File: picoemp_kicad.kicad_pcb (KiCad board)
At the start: 2 copper layers, 40 x 116 mm, 98 parts, among them J1 EDGE-SMA, J2 USB_C_Receptacle_USB2.0, J3 BG306-02-A-2-0400-L-G, J4 Conn_01x02_Pin, P2 Header 2, P3 Header 4, Q1 LDA111STR, Q2 RGT16BM65DTL, Q3 AO3422, Q4 AO3422, Q5 FSS2301S, Q6 FSS2302S, SW1 ARM, SW2 PULSE, SW3 TL3301AF160QJ, SW4 SW_SPST, T1 ATB322524, T2 ATB322524, U1 RP2040, U2 W25Q128JVSIQ, U3 TP4056, U4 DW01A, U5 FS8205A, U6 LP2985-3.3, Y1 X322512MSB4SI

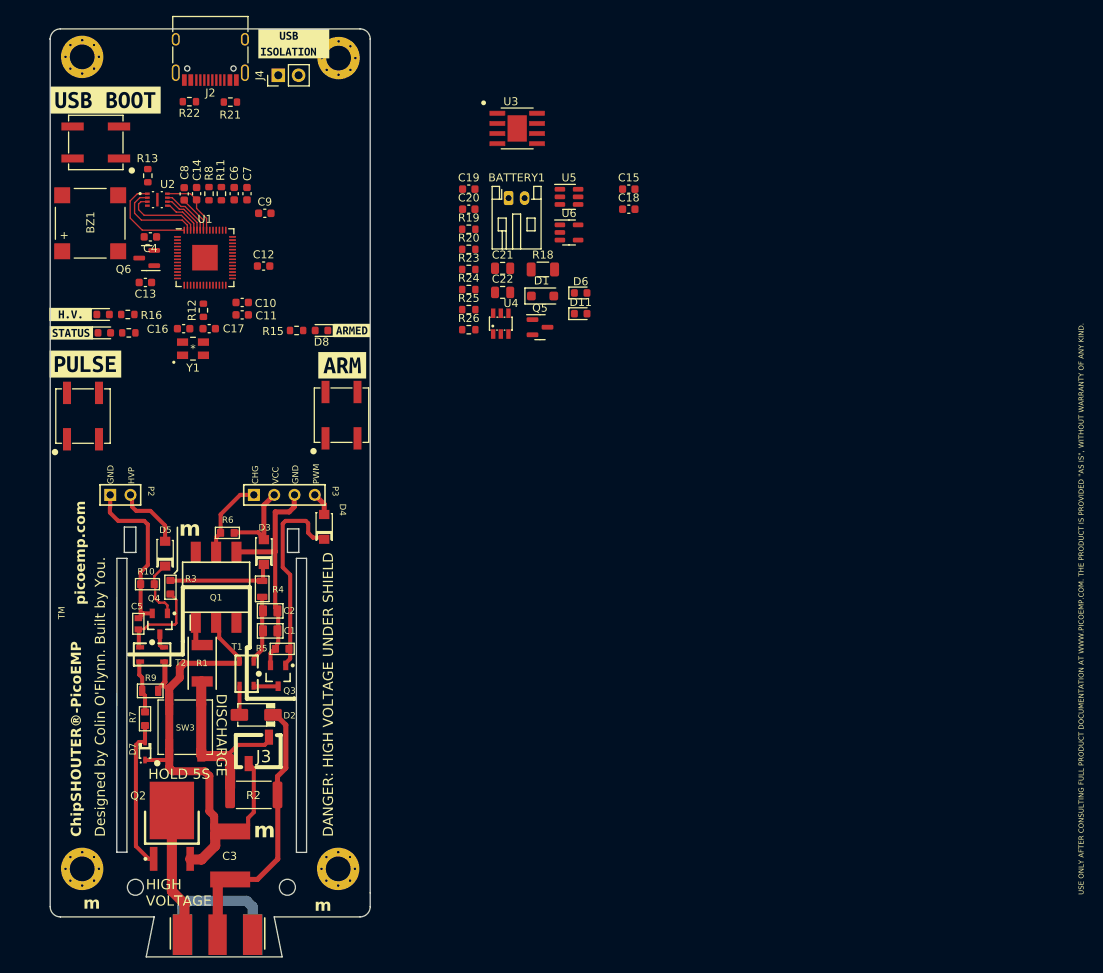
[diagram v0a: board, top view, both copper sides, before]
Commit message: Swapped charging IC for reduced footprint
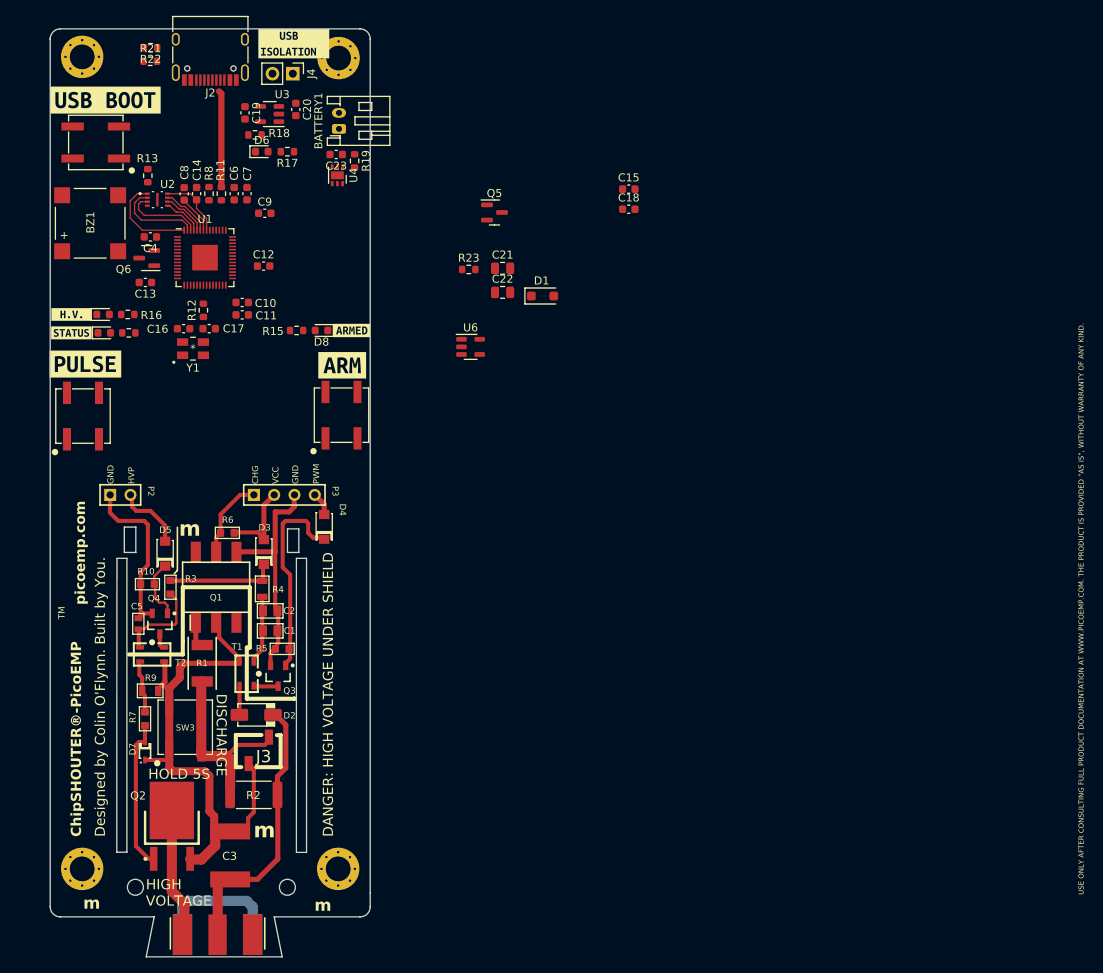
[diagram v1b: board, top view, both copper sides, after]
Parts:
- removed D11: CHARGING, LED_SMD:LED_0603_1608Metric
- removed R20, R24, R26: 1k, Resistor_SMD:R_0603_1608Metric
- removed R25: 100, Resistor_SMD:R_0603_1608Metric
- removed U5: FS8205A, Package_TO_SOT_SMD:SOT-23-6
- removed kibuzzard-63F26E94: G***, kibuzzard-63F26E94
- removed kibuzzard-63F26F80: G***, kibuzzard-63F26F80
- added C23: 100n, Capacitor_SMD:C_0603_1608Metric, F.Cu at (164.3, 62.7)
- added R17: 2k, Resistor_SMD:R_0603_1608Metric, F.Cu at (158.2, 62.4)
- added kibuzzard-63F48B50: G***, kibuzzard-63F48B50, F.Cu at (131.2, 82.7)
- added kibuzzard-63F48B5A: G***, kibuzzard-63F48B5A, F.Cu at (131.2, 85.0)
- C20: value 0.1u -> 10u
- D6: value CHARGING_COMPLETE -> CHARGING
- R18: value 0.4 -> 2k; footprint Resistor_SMD:R_1206_3216Metric -> Resistor_SMD:R_0603_1608Metric
- R19: value 2.2k -> 100
- U3: value TP4056 -> LP4054H; footprint LCSC:SOP127P600X175-9N -> Package_TO_SOT_SMD:SOT-23-5
- U4: value DW01A -> XB6536A; footprint LCSC:SOT23-6 -> Package_DFN_QFN:DFN-6-1EP_2x2mm_P0.65mm_EP1x1.6mm
- moved D6 43.6 mm to (155.0, 62.4)
- moved R18 39.7 mm to (154.1, 60.3), turned to 180 degrees
- moved U3 31.0 mm to (156.0, 57.7), turned to 180 degrees
- moved C19 29.6 mm to (152.9, 57.5), turned to -90 degrees
- moved U4 27.6 mm to (164.4, 65.3), turned to -90 degrees
- moved C20 25.0 mm to (159.2, 57.1), turned to -90 degrees
- moved BATTERY1 22.9 mm to (164.6, 59.5), turned to 90 degrees
- moved U6 18.9 mm to (181.1, 86.8)
- moved R19 16.6 mm to (166.6, 63.5), turned to -90 degrees
- moved Q5 15.4 mm to (184.0, 70.0)
- moved R21 11.2 mm to (141.0, 51.1), turned to 180 degrees
- moved R22 8.31 mm to (141.1, 49.4)
- moved J4 1.83 mm to (158.8, 52.6), turned to -90 degrees
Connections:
- C19 pad 1: /Power/BAT+ -> +5V
- C20 pad 1: Net-(U4-VCC) -> Net-(U3-BAT)
- C20 pad 2: /Power/BAT- -> GND
- D6 pad 2: +5V -> Net-(D6-A)
- R18 pad 1: Net-(U3-VCC) -> Net-(U3-ISET)
- R18 pad 2: +5V -> GND
- R19 pad 1: Net-(U3-PROG) -> /Power/BAT+
- R19 pad 2: GND -> Net-(U4-VDD)
- U3 pad 1: GND -> Net-(D6-K)
- U3 pad 2: Net-(U3-PROG) -> GND
- U3 pad 3: GND -> Net-(U3-BAT)
- U3 pad 4: Net-(U3-VCC) -> +5V
- U3 pad 5: /Power/BAT+ -> Net-(U3-ISET)
- U4 pad 1: Net-(U4-OD) -> Net-(U4-VDD)
- U4 pad 2: Net-(U4-CS) -> /Power/BAT-
- U4 pad 3: Net-(U4-OC) -> /Power/BAT-
- U4 pad 4: unconnected-(U4-TD-Pad4) -> GND
- U4 pad 5: Net-(U4-VCC) -> GND
- U4 pad 6: /Power/BAT- -> GND
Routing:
- net USB_D-: track 0.00 -> 12.1 mm

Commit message: finalized schematic + layout
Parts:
- removed MH2, MH3 (x2): M3, Tight Fit, C:_Users_colin_Dropbox (NewAE Technology Inc)_engineering_altium_Libraries_footprints_MOUNT_M3_TIGHT.PcbLib_MOUNT_M3_TI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
- removed kibuzzard-63F119CF: G***, kibuzzard-63F119CF
- removed kibuzzard-63F26FC0: G***, kibuzzard-63F26FC0
- removed kibuzzard-63F48B50: G***, kibuzzard-63F48B50
- removed kibuzzard-63F48B5A: G***, kibuzzard-63F48B5A
- added C24: 10u, Capacitor_SMD:C_0603_1608Metric, F.Cu at (158.2, 53.1)
- added D10: PICO_LED1, LED_SMD:LED_0603_1608Metric, F.Cu at (156.1, 82.0)
- added D11: LESD9L5.0T5G, Diode_SMD:D_SOD-923, F.Cu at (150.2, 55.2)
- added D13: LESD9L5.0T5G, Diode_SMD:D_SOD-923, F.Cu at (148.1, 55.2)
- added D14: PESDNC5D7VU, Diode_SMD:D_SOD-523, F.Cu at (141.1, 51.2)
- added G***: LOGO, LOGO, F.Cu at (136.3, 155.2)
- added G***: LOGO, LOGO, F.Cu at (160.8, 155.2)
- added G***: LOGO, LOGO, F.Cu at (156.3, 149.1)
- added G***: LOGO, LOGO, F.Cu at (146.8, 108.5)
- added G***: LOGO, LOGO, B.Cu at (149.5, 160.0)
- added J5: Conn_01x03_Socket, Connector_PinHeader_2.54mm:PinHeader_1x03_P2.54mm_Vertical, F.Cu at (154.0, 94.5)
- added J6: Conn_01x08_Socket, Connector_PinSocket_2.54mm:PinSocket_1x08_P2.54mm_Vertical, F.Cu at (130.4, 59.5)
- added MH1: M3, Tight Fit, C:_Users_colin_Dropbox (NewAE Technology Inc)_engineering_altium_Libraries_footprints_MOUNT_M3_TIGHT.PcbLib_MOUNT_M3_TI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, F.Cu at (164.5, 114.7)
- added MH1: M3, Tight Fit, C:_Users_colin_Dropbox (NewAE Technology Inc)_engineering_altium_Libraries_footprints_MOUNT_M3_TIGHT.PcbLib_MOUNT_M3_TI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, F.Cu at (132.5, 114.7)
- added MH1: M3, Tight Fit, C:_Users_colin_Dropbox (NewAE Technology Inc)_engineering_altium_Libraries_footprints_MOUNT_M3_TIGHT.PcbLib_MOUNT_M3_TI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, F.Cu at (164.5, 152.0)
- added MH1: M3, Tight Fit, C:_Users_colin_Dropbox (NewAE Technology Inc)_engineering_altium_Libraries_footprints_MOUNT_M3_TIGHT.PcbLib_MOUNT_M3_TI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, F.Cu at (164.5, 50.5)
- added MH1: M3, Tight Fit, C:_Users_colin_Dropbox (NewAE Technology Inc)_engineering_altium_Libraries_footprints_MOUNT_M3_TIGHT.PcbLib_MOUNT_M3_TI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, F.Cu at (132.5, 50.5)
- added R20: 1k, Resistor_SMD:R_0603_1608Metric, F.Cu at (156.1, 79.0)
- added SW5: SSSS811101, Button_Switch_SMD:SW_SPDT_PCM12, F.Cu at (166.5, 77.7)
- added U5: ME2807, Package_TO_SOT_SMD:SOT-23-3, F.Cu at (166.6, 68.9)
- added U7: LPW5206, Package_TO_SOT_SMD:SOT-23-5, F.Cu at (155.8, 53.7)
- added kibuzzard-63F6135F: G***, kibuzzard-63F6135F, F.Cu at (161.7, 54.6)
- added kibuzzard-63F6135F: G***, kibuzzard-63F6135F, B.Cu at (163.2, 55.8)
- added kibuzzard-63F61A8A: G***, kibuzzard-63F61A8A, F.Cu at (144.5, 92.2)
- added kibuzzard-63F629BA: G***, kibuzzard-63F629BA, F.Cu at (166.0, 72.2)
- added kibuzzard-63F65118: G***, kibuzzard-63F65118, F.Cu at (166.4, 64.7)
- added kibuzzard-63F66756: G***, kibuzzard-63F66756, F.Cu at (140.9, 55.3)
- added kibuzzard-63F66885: G***, kibuzzard-63F66885, F.Cu at (133.8, 59.5)
- added kibuzzard-63F6689E: G***, kibuzzard-63F6689E, F.Cu at (133.8, 62.0)
- added kibuzzard-63F668C9: G***, kibuzzard-63F668C9, F.Cu at (133.9, 77.2)
- added kibuzzard-63F668D5: G***, kibuzzard-63F668D5, F.Cu at (133.8, 74.7)
- added kibuzzard-63F668E9: G***, kibuzzard-63F668E9, F.Cu at (133.8, 64.5)
- added kibuzzard-63F668EF: G***, kibuzzard-63F668EF, F.Cu at (133.8, 67.0)
- added kibuzzard-63F668F6: G***, kibuzzard-63F668F6, F.Cu at (133.8, 69.6)
- added kibuzzard-63F668FC: G***, kibuzzard-63F668FC, F.Cu at (133.8, 72.2)
- added kibuzzard-63F78DFD: G***, kibuzzard-63F78DFD, F.Cu at (167.5, 62.4)
- added kibuzzard-63F78E1E: G***, kibuzzard-63F78E1E, F.Cu at (167.7, 54.6)
- added kibuzzard-63F78E1E: G***, kibuzzard-63F78E1E, B.Cu at (163.8, 57.5)
- added kibuzzard-63FA0F3A: G***, kibuzzard-63FA0F3A, F.Cu at (131.0, 82.7)
- added kibuzzard-63FA1685: G***, kibuzzard-63FA1685, F.Cu at (158.2, 82.7)
- added kibuzzard-63FA16E2: G***, kibuzzard-63FA16E2, F.Cu at (154.7, 87.3)
- added kibuzzard-63FA16E2: G***, kibuzzard-63FA16E2, B.Cu at (154.7, 87.3)
- added kibuzzard-63FA1A3D: G***, kibuzzard-63FA1A3D, F.Cu at (131.0, 85.0)
- added kibuzzard-63FB2541: G***, kibuzzard-63FB2541, B.Cu at (133.9, 59.5)
- added kibuzzard-63FB254D: G***, kibuzzard-63FB254D, B.Cu at (133.9, 62.0)
- added kibuzzard-63FB2554: G***, kibuzzard-63FB2554, B.Cu at (133.9, 64.5)
- added kibuzzard-63FB255A: G***, kibuzzard-63FB255A, B.Cu at (133.9, 67.0)
- added kibuzzard-63FB2562: G***, kibuzzard-63FB2562, B.Cu at (133.9, 69.6)
- added kibuzzard-63FB2568: G***, kibuzzard-63FB2568, B.Cu at (133.9, 72.2)
- added kibuzzard-63FB256F: G***, kibuzzard-63FB256F, B.Cu at (133.9, 74.7)
- added kibuzzard-63FB2575: G***, kibuzzard-63FB2575, B.Cu at (133.8, 77.2)
- added kibuzzard-63FB2610: G***, kibuzzard-63FB2610, F.Cu at (161.6, 101.8)
- added kibuzzard-63FB2610: G***, kibuzzard-63FB2610, B.Cu at (161.6, 101.8)
- added kibuzzard-63FB2711: G***, kibuzzard-63FB2711, F.Cu at (136.0, 101.8)
- added kibuzzard-63FB2711: G***, kibuzzard-63FB2711, F.Cu at (159.1, 101.8)
- added kibuzzard-63FB2711: G***, kibuzzard-63FB2711, B.Cu at (136.0, 101.8)
- added kibuzzard-63FB2711: G***, kibuzzard-63FB2711, B.Cu at (159.1, 101.8)
- added kibuzzard-63FB271A: G***, kibuzzard-63FB271A, F.Cu at (156.5, 101.8)
- added kibuzzard-63FB271A: G***, kibuzzard-63FB271A, B.Cu at (156.5, 101.8)
- added kibuzzard-63FB2724: G***, kibuzzard-63FB2724, F.Cu at (153.9, 101.8)
- added kibuzzard-63FB2724: G***, kibuzzard-63FB2724, B.Cu at (153.9, 101.8)
- added kibuzzard-63FB2766: G***, kibuzzard-63FB2766, F.Cu at (138.6, 101.8)
- added kibuzzard-63FB2766: G***, kibuzzard-63FB2766, B.Cu at (138.5, 101.8)
- added kibuzzard-63FB287B: G***, kibuzzard-63FB287B, F.Cu at (158.2, 89.4)
- added kibuzzard-63FB2882: G***, kibuzzard-63FB2882, F.Cu at (157.4, 92.0)
- added kibuzzard-63FB2887: G***, kibuzzard-63FB2887, F.Cu at (158.2, 94.6)
- added kibuzzard-63FB2899: G***, kibuzzard-63FB2899, B.Cu at (158.2, 89.4)
- added kibuzzard-63FB28A8: G***, kibuzzard-63FB28A8, B.Cu at (157.4, 92.0)
- added kibuzzard-63FB28B5: G***, kibuzzard-63FB28B5, B.Cu at (158.2, 94.6)
- added kibuzzard-63FB3D52: G***, kibuzzard-63FB3D52, B.Cu at (163.8, 59.3)
- added kibuzzard-63FB718C: G***, kibuzzard-63FB718C, F.Cu at (157.7, 47.8)
- BZ1: value Buzzer -> MLT-7525
- C4: value 100m -> 100n
- D1: value RB161MM-20TR -> DS14W
- D3, D4, D5: value SM4005PL-TP -> GOODWORK A7
- R2: value 300K -> 360k
- U6: value LP2985-3.3 -> LP3992-3.3
- moved C18 58.0 mm to (143.0, 66.1), turned to 180 degrees
- moved C15 46.3 mm to (154.8, 72.0)
- moved D1 32.7 mm to (159.4, 69.3), turned to 90 degrees
- moved BZ1 29.5 mm to (146.2, 97.9), turned to 180 degrees
- moved R23 24.8 mm to (157.3, 69.3), turned to -90 degrees
- moved C22 24.7 mm to (161.2, 73.9)
- moved C21 24.1 mm to (161.2, 80.3)
- moved U6 22.1 mm to (161.2, 77.1), turned to 90 degrees
- moved Q5 21.4 mm to (162.6, 69.3)
- moved Q6 17.9 mm to (149.7, 91.1), turned to 0 degrees
- moved D6 8.21 mm to (162.8, 64.7), turned to 180 degrees
- moved U4 7.93 mm to (157.9, 60.8), turned to 180 degrees
- moved SW4 6.86 mm to (140.9, 59.5), turned to 0 degrees
- moved C23 5.58 mm to (158.7, 62.8)
- moved R27 5.05 mm to (137.7, 80.0), turned to -90 degrees
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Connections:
- net Net-(J4-Pin_2) renamed /Power/VBUS
- C20 pad 1: Net-(U3-BAT) -> /Power/BAT+
- C21 pad 1: +5V -> /Power/VOUT
- D3 pad A: VCC -> +3V3
- J4 pad 1: +5V -> Net-(J4-Pin_1)
- P3 pad 2: VCC -> +3V3
- R6 pad 1: VCC -> +3V3
- SW2 pad 1: /RP2040/PULSE_BUTTON -> +3V3
- SW2 pad 2: +3V3 -> /RP2040/PULSE_BUTTON
- U1 pad 18: unconnected-(U1-GPIO15-Pad18) -> /RP2040/BUZZER
- U1 pad 2: unconnected-(U1-GPIO0-Pad2) -> /RP2040/GPIO0
- U1 pad 24: unconnected-(U1-SWCLK-Pad24) -> /RP2040/SWCLK
- U1 pad 25: unconnected-(U1-SWDIO-Pad25) -> /RP2040/SWDIO
- U1 pad 3: unconnected-(U1-GPIO1-Pad3) -> /RP2040/GPIO1
- U1 pad 37: unconnected-(U1-GPIO25-Pad37) -> /RP2040/PICO_LED
- U1 pad 39: unconnected-(U1-GPIO27/ADC1-Pad39) -> /RP2040/ARMED_LED
- U1 pad 4: unconnected-(U1-GPIO2-Pad4) -> /RP2040/GPIO2
- U1 pad 5: unconnected-(U1-GPIO3-Pad5) -> /RP2040/GPIO3
- U1 pad 6: /RP2040/BUZZER -> /RP2040/GPIO4
- U1 pad 7: unconnected-(U1-GPIO5-Pad7) -> /RP2040/GPIO5
- U3 pad 3: Net-(U3-BAT) -> /Power/BAT+
- U6 pad 1: +5V -> /Power/VOUT
- U6 pad 3: +5V -> /Power/LDO_ENABLE
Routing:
- net +3V3: track 8.28 -> 167.4 mm, vias 0 -> 4
- net GND: track 50.5 -> 95.9 mm, vias 0 -> 66
- net CHARGED: track 9.73 -> 44.8 mm
- net /RP2040/ARM_BUTTON: track 0.00 -> 32.5 mm
- net HVPWM: track 2.93 -> 35.5 mm
- net HVPULSE: track 8.83 -> 38.9 mm
- net +5V: track 0.00 -> 26.6 mm
- net /RP2040/PULSE_BUTTON: track 0.00 -> 26.4 mm
- net +1V1: track 4.76 -> 29.9 mm, vias 0 -> 4
- net /Power/VOUT: track 0.00 -> 24.7 mm
- net /RP2040/GPIO0: track 0.00 -> 24.0 mm
- net /RP2040/GPIO1: track 0.00 -> 22.0 mm
- net /Power/VBUS: track 0.00 -> 21.1 mm
- net /RP2040/GPIO2: track 0.00 -> 20.1 mm
- net /RP2040/SWCLK: track 0.00 -> 18.8 mm
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- added copper zone on F.Cu, net +3V3
- added copper zone on F.Cu, net /Power/BAT+
- added copper zone on F.Cu, net /Power/BAT-
- added copper zone on B.Cu, net GND
- added copper zone on F.Cu, net GND
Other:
- board text added: "USE ONLY AFTER CONSULTING FULL PRODUCT DOCUMENTATION AT WWW.PICOEMP.COM THE PRODUCT IS PROVIDED {dblquote}AS IS{dblquote}, WITHOUT WARRANTY OF ANY KIND."
- board text removed: "CHG"
- board text removed: "Designed by Colin O'Flynn. Built by You."
- board text removed: "GND"
- board text removed: "HVP"
- board text removed: "PWM"
- board text removed: "USE ONLY AFTER CONSULTING FULL PRODUCT DOCUMENTATION AT WWW.PICOEMP.COM. THE PRODUCT IS PROVIDED "AS IS", WITHOUT WARRANTY OF ANY KIND."
- board text removed: "VCC"
- board text removed: "m"
- board text removed: "picoemp.com"

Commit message: Small tweaks
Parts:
- added G***: LOGO, LOGO, F.Cu at (135.3, 145.7)
- added G***: LOGO, LOGO, F.Cu at (130.2, 127.7)

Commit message: finishing touches
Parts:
- removed J4: Conn_01x02_Pin, Connector_PinHeader_2.54mm:PinHeader_1x02_P2.54mm_Vertical
- removed the MH1 at (164.5, 50.5)
- removed kibuzzard-63F2728F: G***, kibuzzard-63F2728F
- removed kibuzzard-63FB718C: G***, kibuzzard-63FB718C
- added D15: 5V_PWR, LED_SMD:LED_0603_1608Metric, F.Cu at (134.2, 55.2)
- added G***: LOGO, LOGO, B.Cu at (162.7, 133.3)
- added G***: LOGO, LOGO, B.Cu at (147.6, 133.3)
- added JP1: ~, Jumper:SolderJumper-2_P1.3mm_Open_Pad1.0x1.5mm, B.Cu at (155.1, 52.3)
- added Q7: FSS2302S, Package_TO_SOT_SMD:SOT-23, F.Cu at (158.1, 49.7)
- added R24: 1k, Resistor_SMD:R_0603_1608Metric, F.Cu at (141.1, 48.2)
- added R25: 100k, Resistor_SMD:R_0603_1608Metric, F.Cu at (154.7, 49.7)
- added R26: 100k, Resistor_SMD:R_0603_1608Metric, F.Cu at (143.5, 90.1)
- added REF**: MountingHole_3.2mm_M3_Pad_TopOnly, MountingHole:MountingHole_3.2mm_M3_Pad_TopOnly, F.Cu at (164.5, 50.5)
- added SW6: SSSS811101, Button_Switch_SMD:SW_SPDT_PCM12, B.Cu at (157.9, 49.1)
- added kibuzzard-63FF3009: G***, kibuzzard-63FF3009, F.Cu at (166.2, 85.0)
- added kibuzzard-640062E5: G***, kibuzzard-640062E5, B.Cu at (154.6, 133.3)
- added kibuzzard-640065CA: G***, kibuzzard-640065CA, F.Cu at (130.6, 55.2)
- added kibuzzard-64031476: G***, kibuzzard-64031476, B.Cu at (165.5, 47.8)
- added kibuzzard-640384C5: G***, kibuzzard-640384C5, F.Cu at (149.7, 134.4)
- added kibuzzard-640385A5: G***, kibuzzard-640385A5, F.Cu at (148.6, 143.1)
- added kibuzzard-6403912E: G***, kibuzzard-6403912E, B.Cu at (154.8, 60.3)
- C3: footprint C:_Users_cofly_Dropbox (NewAE Technology Inc)_engineering_altium_Libraries_footprints_CKG57N_2220.PcbLib_CKG57N_2220 -> Capacitor_SMD:C_2220_5650Metric
- moved G*** 1.39 mm to (135.3, 144.3)
- moved G*** 1.39 mm to (130.3, 126.3)
- moved C3 0.81 mm to (151.4, 151.0), turned to 90 degrees
- moved G*** 0.35 mm to (156.7, 149.0)
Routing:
- net +5V: track 26.6 -> 44.3 mm
- net Net-(D15-A): track 0.00 -> 11.3 mm
- net /Power/VBUS: track 21.1 -> 28.6 mm, vias 0 -> 2
- net GND: track 95.9 -> 100.2 mm, vias 66 -> 60
- net Net-(Q7-G): track 0.00 -> 4.15 mm, vias 0 -> 1
- net Net-(JP1-A): track 6.35 -> 9.98 mm, vias 0 -> 1
- net CHARGED: track 44.8 -> 45.6 mm
- net /Power/VOUT: track 24.7 -> 24.1 mm
- net Net-(Q1-K): track 67.2 -> 67.7 mm
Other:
- board text added: "New design by Kevin Pettersson"
- board text added: "Rev: V1"
- board text added: "Speical thanks to Colin O'Flynn for the original design!"
- board text removed: "DISCHARGE"
- board text removed: "HOLD 5S"
- board text removed: "USE ONLY AFTER CONSULTING FULL PRODUCT DOCUMENTATION AT WWW.PICOEMP.COM THE PRODUCT IS PROVIDED {dblquote}AS IS{dblquote}, WITHOUT WARRANTY OF ANY KIND."
